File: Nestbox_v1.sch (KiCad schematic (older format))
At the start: 24 parts, among them P1 RX/TX, P2 TST/RST, P3 VDD/GND, Q1 SFH 3605, SW1 SMD-BUTTON_2P-3.0X2.5X1.2+0.4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, U1 MSP430FR5969, Y1 Crystal

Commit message: pcb file components clustering
pcb file components were clustered according to the Eeschema -
currently everything is on one layer, F.Cu
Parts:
- D1: symbol LED -> LED-RESCUE-Nestbox_v1
- RV1: symbol POT -> POT-RESCUE-Nestbox_v1
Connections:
- no-connect marks 22 -> 23
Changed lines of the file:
@@
 EESchema Schematic File Version 2
+LIBS:Nestbox_v1-rescue
 LIBS:power
 LIBS:device
@@
 LIBS:contrib
 LIBS:valves
-LIBS:octanis3
 LIBS:SeeedOPL-Capacitor-2016
 LIBS:SeeedOPL-Connector-2016
@@
 LIBS:SeeedOPL-Switch-2016
 LIBS:SeeedOPL-Transistor-2016
-LIBS:crystal_4pin
 LIBS:Nestbox_v1-cache
 EELAYER 25 0
@@
 Concerning GPIOs:\nThe maximum total current, \nI(OHmax) and I(OLmax), \nfor all outputs combined should\nnot exceed ±48 mA(100 mA) to \nhold the maximum voltage drop \nof 0.25V (0.6V).
 $Comp
-L LED D1
+L LED-RESCUE-Nestbox_v1 D1
 U 1 1 587A720E
 P 650 4250
@@
 $EndComp
 $Comp
-L POT RV1
+L POT-RESCUE-Nestbox_v1 RV1
 U 1 1 587B63C8
 P 1400 3800
@@
 Wire Wire Line
 	3150 1750 3150 1800
+NoConn ~ 1500 5800
 $EndSCHEMATC

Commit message: circular NFC antenna added to pcb file, as well as other important changes and additions of library components
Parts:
- removed C4: CERAMIC-10UF-10V-_-20%~+80%_-Y5V_0805_, SeeedOPL-Capacitor-2016:C0805, symbol CERAMIC-10UF-10V-_-20%~+80%_-Y5V_0805_
- added C4: CERAMIC-10UF-25V-10%-X5R_0805_, SeeedOPL-Capacitor-2016:C0805, symbol CERAMIC-10UF-25V-10%-X5R_0805_
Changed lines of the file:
@@
 LIBS:contrib
 LIBS:valves
+LIBS:octanis3
 LIBS:SeeedOPL-Capacitor-2016
 LIBS:SeeedOPL-Connector-2016
@@
 Wire Wire Line
 	5350 1550 5350 1800
-$Comp
-L CERAMIC-10UF-10V-_-20%~+80%_-Y5V_0805_ C4
-U 1 1 587CBE57
-P 5150 1750
-F 0 "C4" H 5000 1800 45  0000 L BNN
-F 1 "CERAMIC-10UF-10V-_-20%~+80%_-Y5V_0805_" H 5000 1650 45  0000 L BNN
-F 2 "SeeedOPL-Capacitor-2016:C0805" H 5150 1750 60  0001 C CNN
-F 3 "" H 5150 1750 60  0001 C CNN
-F 4 "CC0805ZKY5V6BB106" H 5180 1900 20  0001 C CNN "MPN"
-F 5 "302010158" H 5180 1900 20  0001 C CNN "SKU"
-	1    5150 1750
-	1    0    0    -1
-$EndComp
 Wire Wire Line
 	5300 1750 5350 1750
@@
 	3150 1750 3150 1800
 NoConn ~ 1500 5800
+$Comp
+L CERAMIC-10UF-25V-10%-X5R_0805_ C4
+U 1 1 58B8E196
+P 5150 1750
+F 0 "C4" H 5000 1800 45  0000 L BNN
+F 1 "CERAMIC-10UF-25V-10%-X5R_0805_" H 5000 1650 45  0000 L BNN
+F 2 "SeeedOPL-Capacitor-2016:C0805" H 5150 1750 60  0001 C CNN
+F 3 "" H 5150 1750 60  0001 C CNN
+F 4 "CC0805KKX5R8BB106" H 5180 1900 20  0001 C CNN "MPN"
+F 5 "302010178" H 5180 1900 20  0001 C CNN "SKU"
+	1    5150 1750
+	1    0    0    -1
+$EndComp
 $EndSCHEMATC

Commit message: added lora component
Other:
- note removed: "to be added later...\n"
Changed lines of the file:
@@
 $Descr A4 11693 8268
 encoding utf-8
-Sheet 1 3
+Sheet 1 4
 Title "Octanis 3 Nestbox"
 Date ""
@@
 	-1   0    0    1
 $EndComp
-Text GLabel 7200 5750 2    60   Input ~ 0
-LORA_TX
 Text GLabel 7200 5850 2    60   Input ~ 0
 LORA_RX
-Text Notes 7700 5850 0    60   ~ 0
-to be added later...\n
 $Comp
 L +BATT #PWR022
@@
 	1    0    0    -1
 $EndComp
+Text GLabel 7200 5750 2    60   Input ~ 0
+LORA_TX
+$Sheet
+S 7750 5650 1300 600
+U 58B94629
+F0 "nestbox_lora" 60
+F1 "nestbox_lora.sch" 60
+$EndSheet
 $EndSCHEMATC

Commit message: finished component placement incl. LoRa
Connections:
- net LORA_RST_N: now reaches U1.35 (P4.6)
- no-connect marks 23 -> 22
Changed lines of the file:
@@
 	-1   0    0    1
 $EndComp
-NoConn ~ 6850 3200
 NoConn ~ 6850 3300
 NoConn ~ 6850 3400
@@
 F1 "nestbox_lora.sch" 60
 $EndSheet
+Wire Wire Line
+	6850 3200 7300 3200
+Text GLabel 7300 3200 2    60   Input ~ 0
+LORA_RST_N
 $EndSCHEMATC

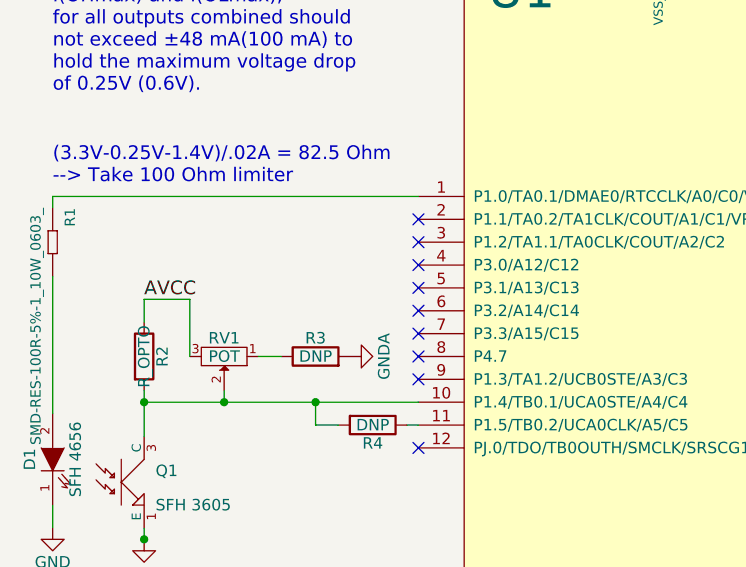
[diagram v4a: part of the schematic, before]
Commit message: added additional connector for light barrier
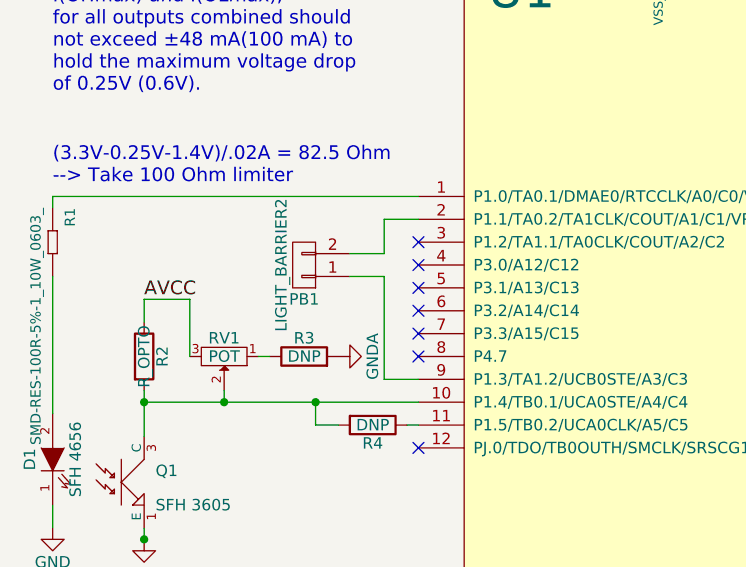
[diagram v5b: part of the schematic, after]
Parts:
- added PB1: LIGHT_BARRIER2, Socket_Strips:Socket_Strip_Straight_1x02, symbol CONN_01X02
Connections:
- net at U1.2 (P1.1/TA0.2/TA1CLK/COUT/A1/C1/VREF+/VeREF+): now also PB1.2 (P2)
- net at U1.9 (P1.3/TA1.2/UCB0STE/A3/C3): now also PB1.1 (P1)
- no-connect marks 22 -> 20
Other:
- moved on the sheet: R3
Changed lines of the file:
@@
 L R R3
 U 1 1 587B6600
-P 1800 3800
-F 0 "R3" V 1880 3800 50  0000 C CNN
-F 1 "DNP" V 1800 3800 50  0000 C CNN
-F 2 "Resistors_SMD:R_0603" V 1730 3800 50  0001 C CNN
-F 3 "" H 1800 3800 50  0000 C CNN
-	1    1800 3800
+P 1750 3800
+F 0 "R3" V 1830 3800 50  0000 C CNN
+F 1 "DNP" V 1750 3800 50  0000 C CNN
+F 2 "Resistors_SMD:R_0603" V 1680 3800 50  0001 C CNN
+F 3 "" H 1750 3800 50  0000 C CNN
+	1    1750 3800
 	0    -1   -1   0
 $EndComp
@@
 L GNDA #PWR011
 U 1 1 587B665F
-P 1950 3800
-F 0 "#PWR011" H 1950 3550 50  0001 C CNN
-F 1 "GNDA" H 1950 3650 50  0000 C CNN
-F 2 "" H 1950 3800 50  0000 C CNN
-F 3 "" H 1950 3800 50  0000 C CNN
-	1    1950 3800
+P 1900 3800
+F 0 "#PWR011" H 1900 3550 50  0001 C CNN
+F 1 "GNDA" H 1900 3650 50  0000 C CNN
+F 2 "" H 1900 3800 50  0000 C CNN
+F 3 "" H 1900 3800 50  0000 C CNN
+	1    1900 3800
 	0    -1   -1   0
 $EndComp
@@
 NoConn ~ 4000 5800
 NoConn ~ 3900 5800
-NoConn ~ 2250 3200
 NoConn ~ 2250 3300
 NoConn ~ 2250 3400
@@
 NoConn ~ 2250 3700
 NoConn ~ 2250 3800
-NoConn ~ 2250 3900
 NoConn ~ 2250 4200
 NoConn ~ 4400 1800
@@
 Connection ~ 1400 4000
 Wire Wire Line
-	1650 3800 1550 3800
+	1600 3800 1550 3800
 Wire Wire Line
 	650  4550 650  4450
@@
 Text GLabel 7300 3200 2    60   Input ~ 0
 LORA_RST_N
+$Comp
+L CONN_01X02 PB1
+U 1 1 58BA717E
+P 1750 3400
+F 0 "PB1" H 1750 3550 50  0000 C CNN
+F 1 "LIGHT_BARRIER2" V 1850 3400 50  0000 C CNN
+F 2 "Socket_Strips:Socket_Strip_Straight_1x02" H 1750 3400 50  0001 C CNN
+F 3 "" H 1750 3400 50  0000 C CNN
+	1    1750 3400
+	-1   0    0    1
+$EndComp
+Wire Wire Line
+	2250 3900 2100 3900
+Wire Wire Line
+	2100 3900 2100 3450
+Wire Wire Line
+	2100 3450 1950 3450
+Wire Wire Line
+	2250 3200 2100 3200
+Wire Wire Line
+	2100 3200 2100 3350
+Wire Wire Line
+	2100 3350 1950 3350
 $EndSCHEMATC

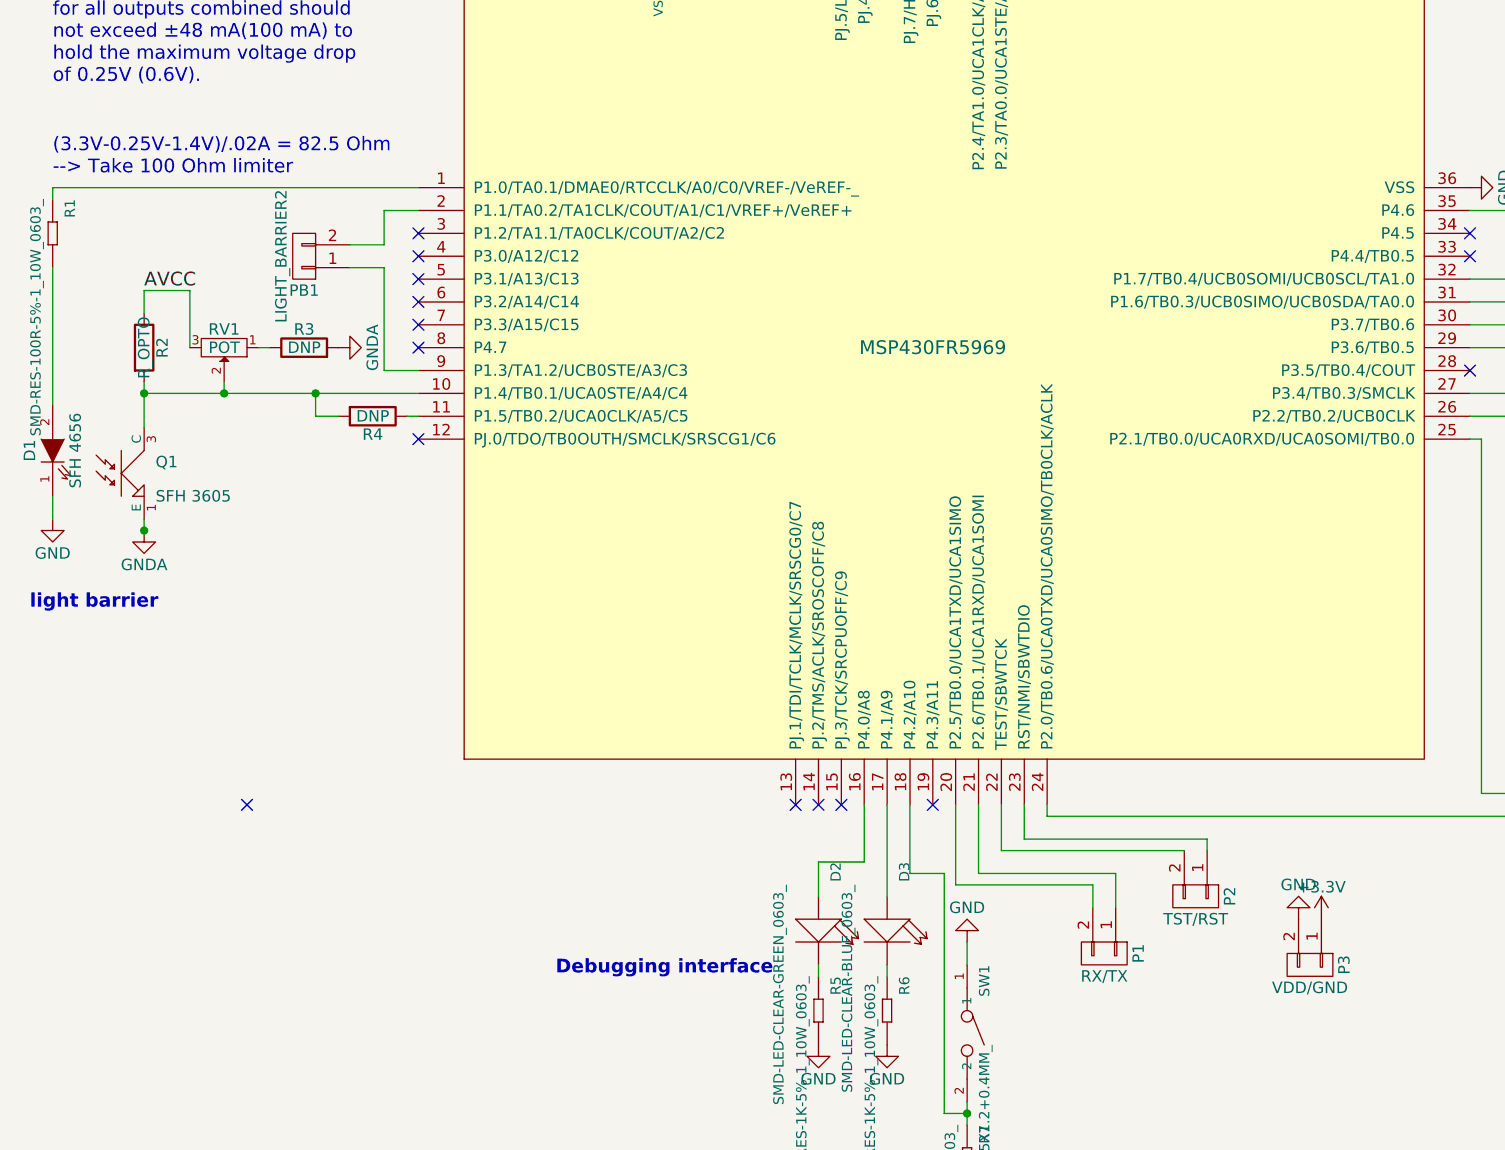
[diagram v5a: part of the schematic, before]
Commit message: corrected phototransistor pins, added power jumpers & testpoints and light barrier signal access
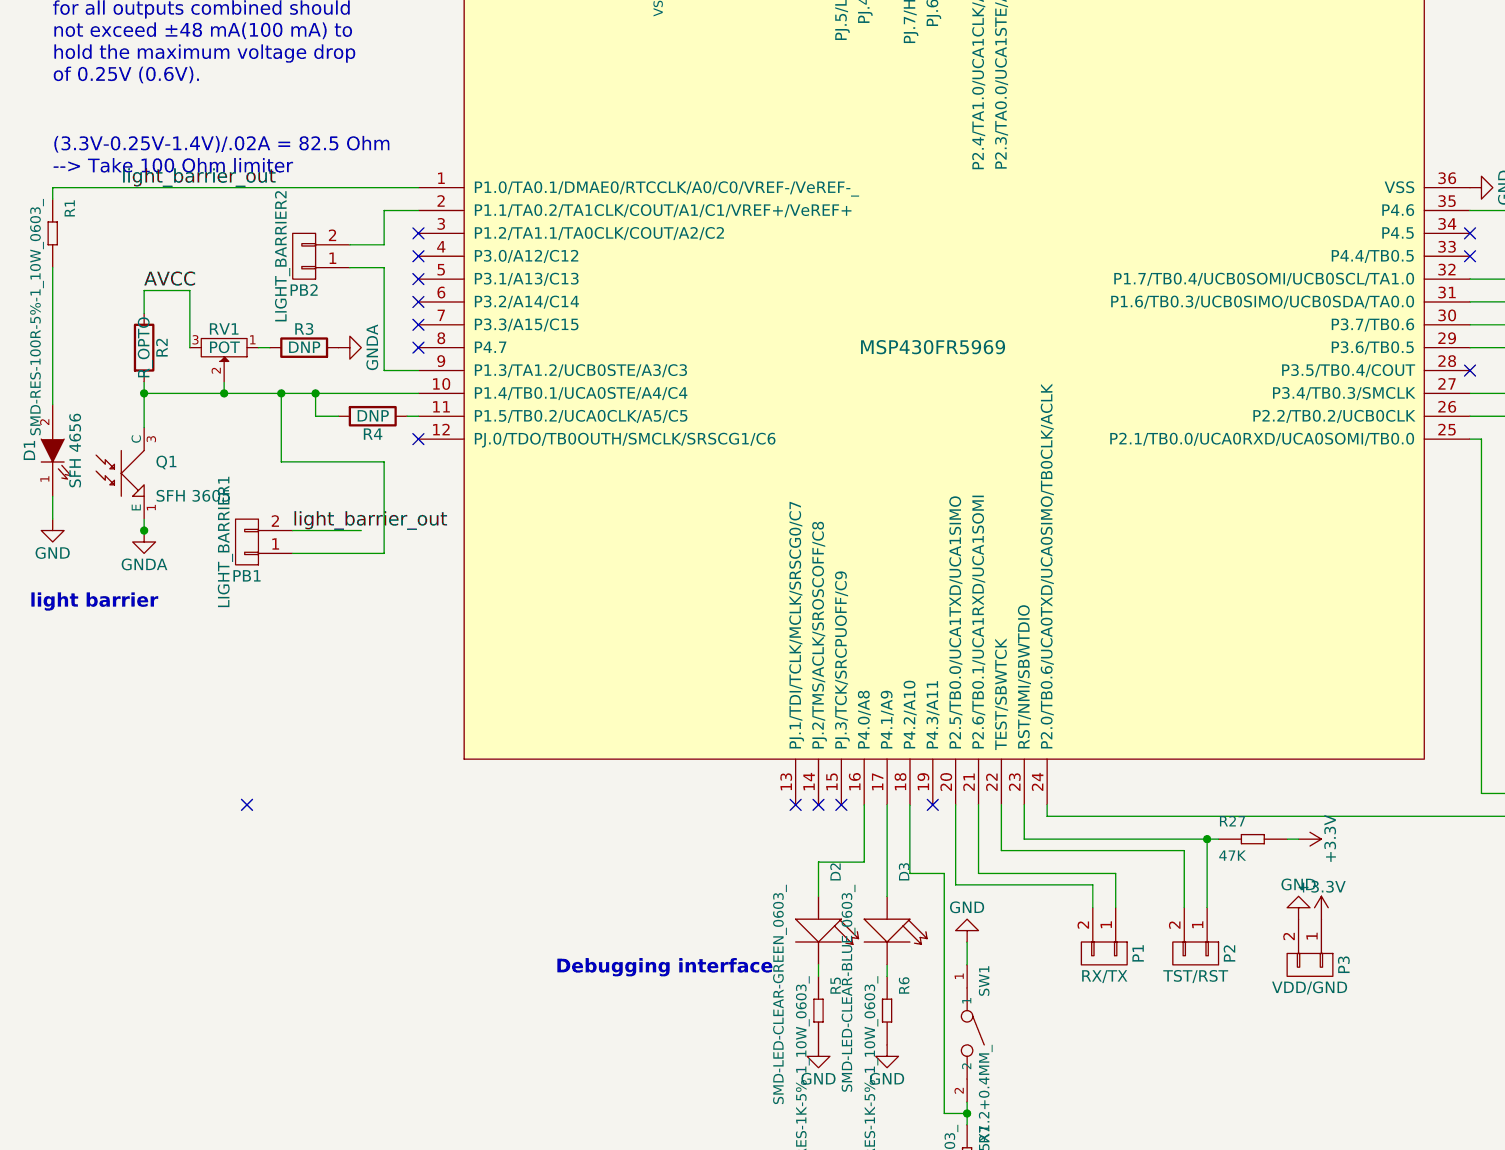
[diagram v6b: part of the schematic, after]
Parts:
- added PB1: LIGHT_BARRIER1, Socket_Strips:Socket_Strip_Straight_1x02, symbol CONN_01X02
- added R27: 47K, SeeedOPL-Resistor-2016:R0603, symbol DIP-RES-47K-5%-1_4W_PR-D2.3XL6.5MM_
- renumbered PB1 to PB2
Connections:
- net +3V3: now also R27.2
- net light_barrier_out: now reaches R1.1, U1.1 (P1.0/TA0.1/DMAE0/RTCCLK/A0/C0/VREF-/VeREF-_)
- net light_barrier_out: now also PB1.2 (P2)
- net at Q1.3 (C), R2.2, R4.2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: now also PB1.1 (P1)
- net at P2.1 (P1), U1.23 (RST/NMI/SBWTDIO): now also R27.1
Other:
- moved on the sheet: P2
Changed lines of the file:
@@
 L CONN_01X02 P2
 U 1 1 58653CFC
-P 5650 6200
-F 0 "P2" H 5650 6350 50  0000 C CNN
-F 1 "TST/RST" V 5750 6200 50  0000 C CNN
-F 2 "Socket_Strips:Socket_Strip_Straight_1x02" H 5650 6200 50  0001 C CNN
-F 3 "" H 5650 6200 50  0000 C CNN
-	1    5650 6200
+P 5650 6450
+F 0 "P2" H 5650 6600 50  0000 C CNN
+F 1 "TST/RST" V 5750 6450 50  0000 C CNN
+F 2 "Socket_Strips:Socket_Strip_Straight_1x02" H 5650 6450 50  0001 C CNN
+F 3 "" H 5650 6450 50  0000 C CNN
+	1    5650 6450
 	0    1    1    0
 $EndComp
@@
 	4800 5800 4800 6000
 Wire Wire Line
-	4800 6000 5600 6000
-Wire Wire Line
 	4900 5800 4900 5950
 Wire Wire Line
-	4900 5950 5700 5950
-Wire Wire Line
-	5700 5950 5700 6000
+	4900 5950 5750 5950
+Wire Wire Line
+	5700 5950 5700 6250
 Wire Wire Line
 	4650 7100 4650 7200
@@
 LORA_RST_N
 $Comp
-L CONN_01X02 PB1
+L CONN_01X02 PB2
 U 1 1 58BA717E
 P 1750 3400
-F 0 "PB1" H 1750 3550 50  0000 C CNN
+F 0 "PB2" H 1750 3550 50  0000 C CNN
 F 1 "LIGHT_BARRIER2" V 1850 3400 50  0000 C CNN
 F 2 "Socket_Strips:Socket_Strip_Straight_1x02" H 1750 3400 50  0001 C CNN
@@
 Wire Wire Line
 	2100 3350 1950 3350
+Wire Wire Line
+	4800 6000 5600 6000
+Wire Wire Line
+	5600 6000 5600 6250
+$Comp
+L +3.3V #PWR031
+U 1 1 58BC4BB7
+P 6100 5950
+F 0 "#PWR031" H 6100 5800 50  0001 C CNN
+F 1 "+3.3V" H 6100 6090 50  0000 C CNN
+F 2 "" H 6100 5950 50  0000 C CNN
+F 3 "" H 6100 5950 50  0000 C CNN
+	1    6100 5950
+	0    1    1    0
+$EndComp
+$Comp
+L DIP-RES-47K-5%-1_4W_PR-D2.3XL6.5MM_ R27
+U 1 1 58BC590C
+P 5900 5950
+F 0 "R27" H 5750 6000 45  0000 L BNN
+F 1 "47K" H 5750 5850 45  0000 L BNN
+F 2 "SeeedOPL-Resistor-2016:R0603" H 5900 5950 40  0001 C CNN
+F 3 "" H 5900 5950 40  0001 C CNN
+F 4 "FHCFR-1_4W-473J" H 5930 6100 20  0001 C CNN "MPN"
+	1    5900 5950
+	1    0    0    -1
+$EndComp
+Connection ~ 5700 5950
+Wire Wire Line
+	6100 5950 6050 5950
+$Comp
+L CONN_01X02 PB1
+U 1 1 58BC974F
+P 1500 4650
+F 0 "PB1" H 1500 4800 50  0000 C CNN
+F 1 "LIGHT_BARRIER1" V 1600 4650 50  0000 C CNN
+F 2 "Socket_Strips:Socket_Strip_Straight_1x02" H 1500 4650 50  0001 C CNN
+F 3 "" H 1500 4650 50  0000 C CNN
+	1    1500 4650
+	-1   0    0    1
+$EndComp
+Wire Wire Line
+	1650 4000 1650 4300
+Wire Wire Line
+	1650 4300 2100 4300
+Wire Wire Line
+	2100 4300 2100 4700
+Wire Wire Line
+	2100 4700 1700 4700
+Connection ~ 1650 4000
+Text Label 950  3100 0    60   ~ 0
+light_barrier_out
+Wire Wire Line
+	1700 4600 2000 4600
+Text Label 1700 4600 0    60   ~ 0
+light_barrier_out
 $EndSCHEMATC
